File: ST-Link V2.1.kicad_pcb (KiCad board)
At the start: 2 copper layers, 46 x 20.6 mm, 45 parts, among them J1 USB_OTG, J2 Conn_01x06, J3 Conn_01x08, J4 Conn_01x08, Q1 MMBT3904, U1 USBLC6-2SC6, U2 stm32, U3 MIC5219-3.3, X1 8MHz

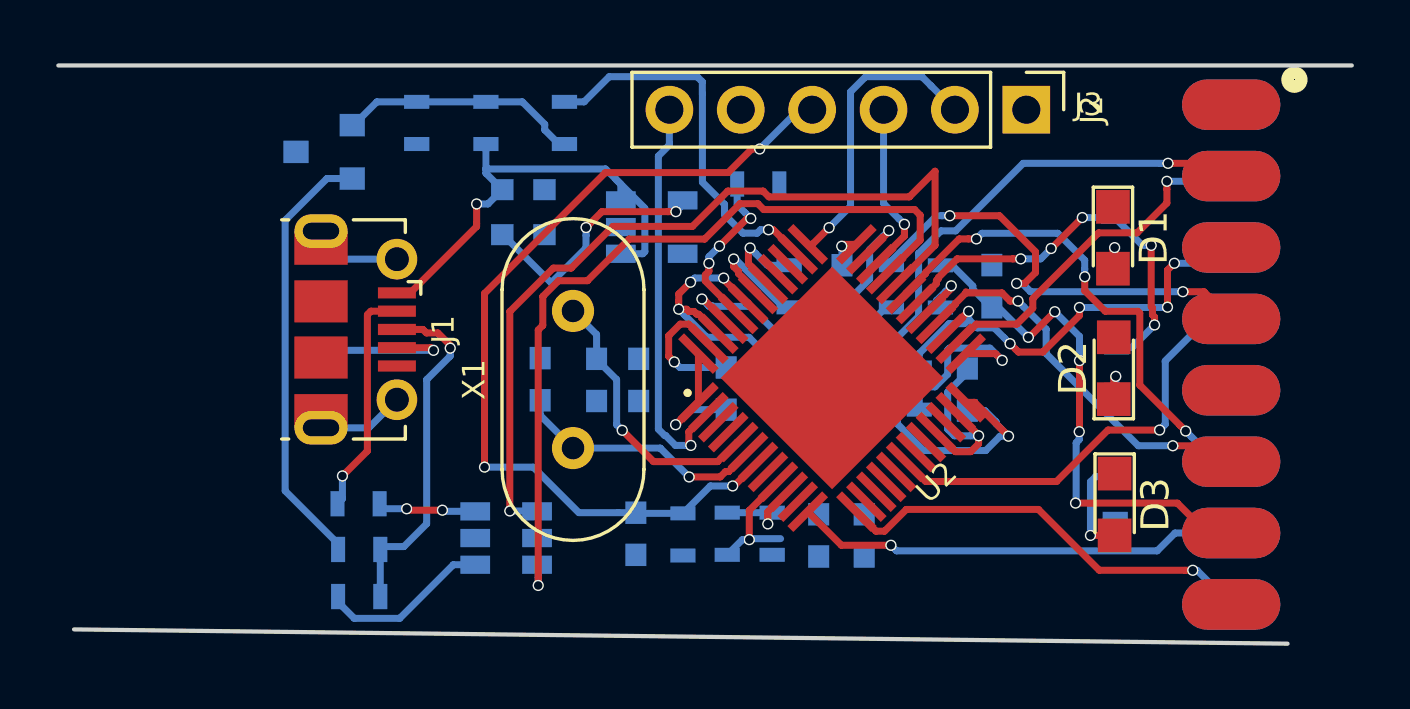
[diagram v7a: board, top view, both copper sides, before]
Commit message: routing all done (33.5mm X 21.1mm)
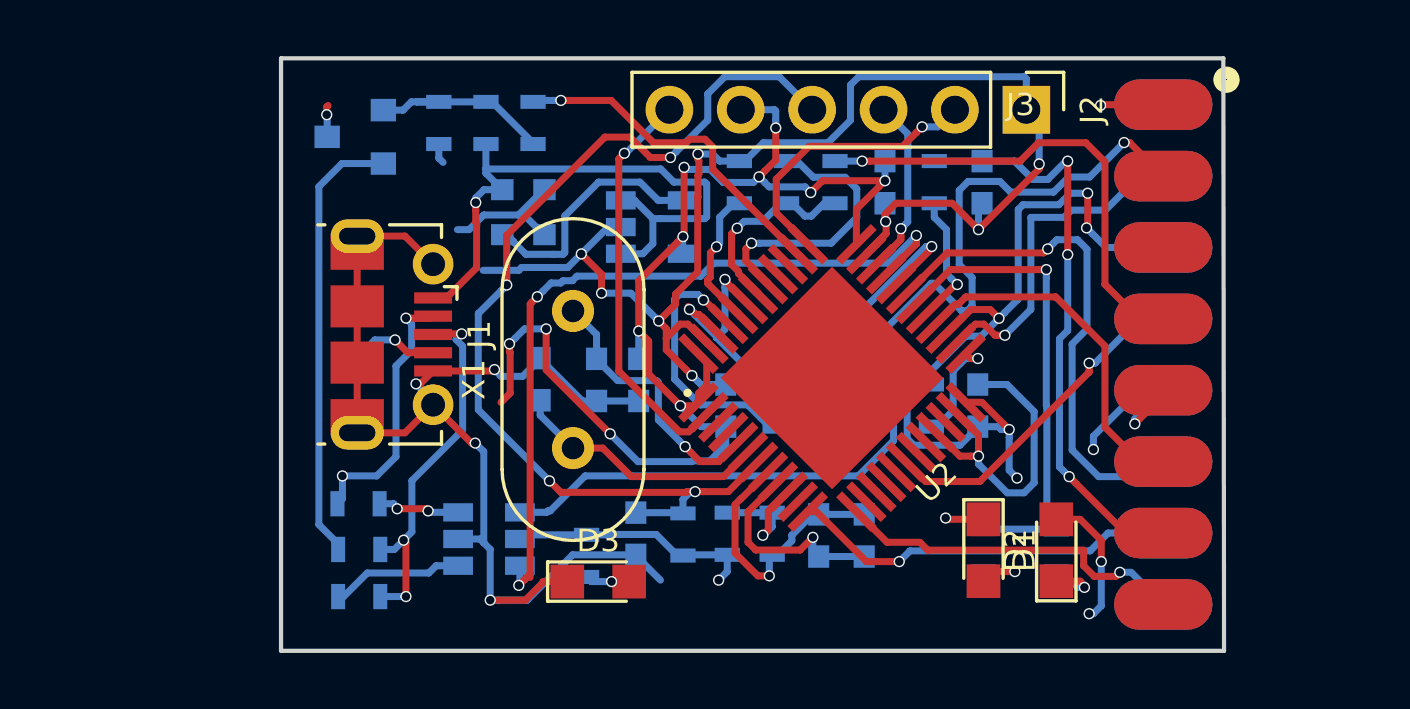
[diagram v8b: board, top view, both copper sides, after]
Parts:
- moved R16 18.9 mm to (129.0, 115.7), turned to 90 degrees
- moved D3 18.6 mm to (129.4, 116.7), turned to 0 degrees
- moved R12 12.0 mm to (143.1, 115.5)
- moved D1 12.0 mm to (143.1, 115.5)
- moved R13 6.82 mm to (145.7, 115.6)
- moved D2 6.79 mm to (145.7, 115.5)
- moved R21 4.21 mm to (137.8, 102.5)
- moved C5 4.01 mm to (139.6, 102.5)
- moved R15 3.72 mm to (141.4, 102.5)
- moved C7 3.72 mm to (143.1, 102.5), turned to 270 degrees
- moved R18 3.71 mm to (136.1, 102.5)
- moved J3 2.42 mm to (149.5, 99.7)
- moved J4 2.42 mm to (149.5, 99.7)
- moved J1 1.30 mm to (121.2, 107.9)
- moved Q1 1.23 mm to (120.8, 100.8)
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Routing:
- net GND: track 23.2 -> 124.5 mm, vias 3 -> 16
- net /3V3_ST_LINK: track 22.9 -> 84.9 mm, vias 4 -> 20
- net /SWIM_RST_IN: track 3.24 -> 10.1 mm
- net +5V: track 17.1 -> 22.3 mm
- net /NRST: track 31.7 -> 36.4 mm, vias 3 -> 4
- net /T_NRST: track 15.6 -> 12.0 mm
- net /MCO: track 18.8 -> 22.0 mm, vias 5 -> 3
- net /STLINK_RX: track 15.3 -> 12.7 mm
- net /LED_STLINK: track 14.7 -> 17.3 mm, vias 5 -> 1
- net Net-(R15-Pad2): track 2.22 -> 4.78 mm
- net /T_SWDIO_IN: track 6.24 -> 3.99 mm
- net Net-(J1-Pad4): track 4.89 -> 2.89 mm
- net /USB_DM: track 30.0 -> 28.1 mm
- net Net-(Q1-Pad1): track 8.63 -> 6.84 mm
- net /SWIM: track 11.4 -> 13.2 mm
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- added copper zone on F.Cu, net /3V3_ST_LINK
- added copper zone on B.Cu, net GND
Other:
- board size 46 x 20.6 mm -> 33.6 x 21.1 mm
- net class Default: via_dia 0.6 -> 0.4; via_drill 0.4 -> 0.3
